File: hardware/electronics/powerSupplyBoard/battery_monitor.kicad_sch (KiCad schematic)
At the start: 34 parts, among them J10 1729018, J9 S3B-XH-SM4-TB, Q2 CSD18532Q5B, Q3 CSD18532Q5B, U5 BQ76905

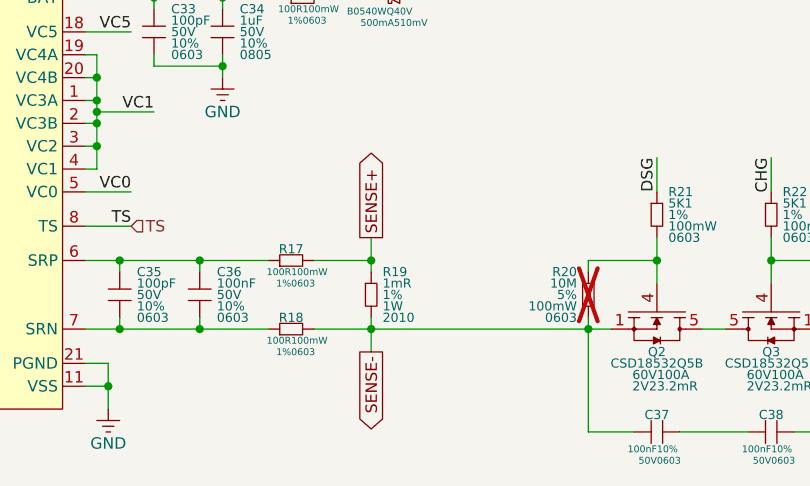
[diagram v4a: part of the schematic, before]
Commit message: recalculated Rsense
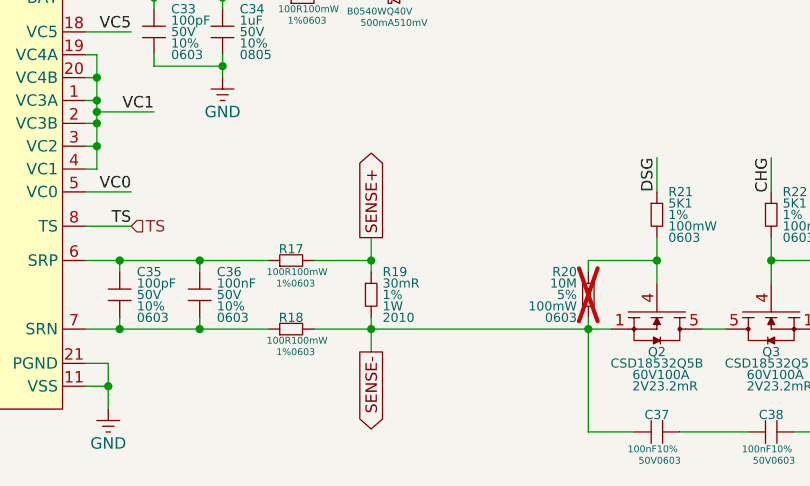
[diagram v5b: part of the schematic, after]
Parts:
- R19: value 1mR -> 30mR; DKPN WSLF-.001CT-ND -> WSLF-.03CT-ND; MPN WSL20101L000FEA18 -> WSL2010R0300FEA18
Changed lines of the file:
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@@
 	)
 	(symbol
-		(lib_id "lib_sch:R")
-		(at 158.75 121.92 0)
-		(unit 1)
-		(exclude_from_sim no)
-		(in_bom yes)
-		(on_board yes)
-		(dnp no)
-		(property "Reference" "R19"
-			(at 160.02 119.38 0)
-			(do_not_autoplace yes)
-			(effects
-				(font
-					(size 1.016 1.016)
-				)
-				(justify left)
-			)
-		)
-		(property "Value" "1mR"
-			(at 160.02 120.65 0)
-			(do_not_autoplace yes)
-			(effects
-				(font
-					(size 1.016 1.016)
-				)
-				(justify left)
-			)
-		)
-		(property "Footprint" "DS-Resistors-SMD:WSLHP2010"
-			(at 158.75 119.38 0)
-			(effects
-				(font
-					(size 1.27 1.27)
-				)
-				(hide yes)
-			)
-		)
-		(property "Datasheet" "datasheets/Vishay-Dale-WSL-HP.pdf"
-			(at 158.75 119.38 0)
-			(effects
-				(font
-					(size 1.27 1.27)
-				)
-				(hide yes)
-			)
-		)
-		(property "Description" "RES 0.001 OHM 1% 1W 2010"
-			(at 158.75 121.92 0)
-			(effects
-				(font
-					(size 1.27 1.27)
-				)
-				(hide yes)
-			)
-		)
-		(property "Manufacturer" "Vishay Dale"
-			(at 158.75 119.38 0)
-			(effects
-				(font
-					(size 1.27 1.27)
-				)
-				(hide yes)
-			)
-		)
-		(property "MPN" "WSL20101L000FEA18"
-			(at 158.75 119.38 0)
-			(effects
-				(font
-					(size 1.27 1.27)
-				)
-				(hide yes)
-			)
-		)
-		(property "DKPN" "WSLF-.001CT-ND"
-			(at 158.75 121.92 0)
-			(effects
-				(font
-					(size 1.27 1.27)
-				)
-				(hide yes)
-			)
-		)
-		(property "Tolerance" "1%"
-			(at 160.02 121.92 0)
-			(do_not_autoplace yes)
-			(effects
-				(font
-					(size 1.016 1.016)
-				)
-				(justify left)
-			)
-		)
-		(property "Power Rating" "1W"
-			(at 160.02 123.19 0)
-			(do_not_autoplace yes)
-			(effects
-				(font
-					(size 1.016 1.016)
-				)
-				(justify left)
-			)
-		)
-		(property "Package" "2010"
-			(at 160.02 124.46 0)
-			(do_not_autoplace yes)
-			(effects
-				(font
-					(size 1.016 1.016)
-				)
-				(justify left)
-			)
-		)
-		(pin "1"
-		)
-		(pin "2"
-		)
-		(instances
-			(project "powerSupplyBoard"
-				(path "/6f3ae1d2-e925-4178-b812-ea14ec542b6c/ec26ef98-8e8c-46d6-a822-e7ed17aae681"
-					(reference "R19")
-					(unit 1)
-				)
-			)
-		)
-	)
-	(symbol
 		(lib_id "lib_sch:GND")
 		(at 81.28 99.06 0)
@@
 					(unit 1)
 				)
+			)
+		)
+	)
+	(symbol
+		(lib_id "lib_sch:R")
+		(at 158.75 121.92 0)
+		(unit 1)
+		(exclude_from_sim no)
+		(in_bom yes)
+		(on_board yes)
+		(dnp no)
+		(property "Reference" "R19"
+			(at 160.02 119.38 0)
+			(do_not_autoplace yes)
+			(effects
+				(font
+					(size 1.016 1.016)
+				)
+				(justify left)
+			)
+		)
+		(property "Value" "30mR"
+			(at 160.02 120.65 0)
+			(do_not_autoplace yes)
+			(effects
+				(font
+					(size 1.016 1.016)
+				)
+				(justify left)
+			)
+		)
+		(property "Footprint" "DS-Resistors-SMD:WSLHP2010"
+			(at 158.75 119.38 0)
+			(effects
+				(font
+					(size 1.27 1.27)
+				)
+				(hide yes)
+			)
+		)
+		(property "Datasheet" "datasheets/Vishay-Dale-WSL-HP.pdf"
+			(at 158.75 119.38 0)
+			(effects
+				(font
+					(size 1.27 1.27)
+				)
+				(hide yes)
+			)
+		)
+		(property "Description" "RES 0.03 OHM 1% 1W 2010"
+			(at 158.75 121.92 0)
+			(effects
+				(font
+					(size 1.27 1.27)
+				)
+				(hide yes)
+			)
+		)
+		(property "Manufacturer" "Vishay Dale"
+			(at 158.75 119.38 0)
+			(effects
+				(font
+					(size 1.27 1.27)
+				)
+				(hide yes)
+			)
+		)
+		(property "MPN" "WSL2010R0300FEA18"
+			(at 158.75 119.38 0)
+			(effects
+				(font
+					(size 1.27 1.27)
+				)
+				(hide yes)
+			)
+		)
+		(property "DKPN" "WSLF-.03CT-ND"
+			(at 158.75 121.92 0)
+			(effects
+				(font
+					(size 1.27 1.27)
+				)
+				(hide yes)
+			)
+		)
+		(property "Tolerance" "1%"
+			(at 160.02 121.92 0)
+			(do_not_autoplace yes)
+			(effects
+				(font
+					(size 1.016 1.016)
+				)
+				(justify left)
+			)
+		)
+		(property "Power Rating" "1W"
+			(at 160.02 123.19 0)
+			(do_not_autoplace yes)
+			(effects
+				(font
+					(size 1.016 1.016)
+				)
+				(justify left)
+			)
+		)
+		(property "Package" "2010"
+			(at 160.02 124.46 0)
+			(do_not_autoplace yes)
+			(effects
+				(font
+					(size 1.016 1.016)
+				)
+				(justify left)
+			)
+		)
+		(pin "1"
+		)
+		(pin "2"
+		)
+		(instances
+			(project "powerSupplyBoard"
+				(path "/6f3ae1d2-e925-4178-b812-ea14ec542b6c/ec26ef98-8e8c-46d6-a822-e7ed17aae681"
+					(reference "R19")
+					(unit 1)
+				)

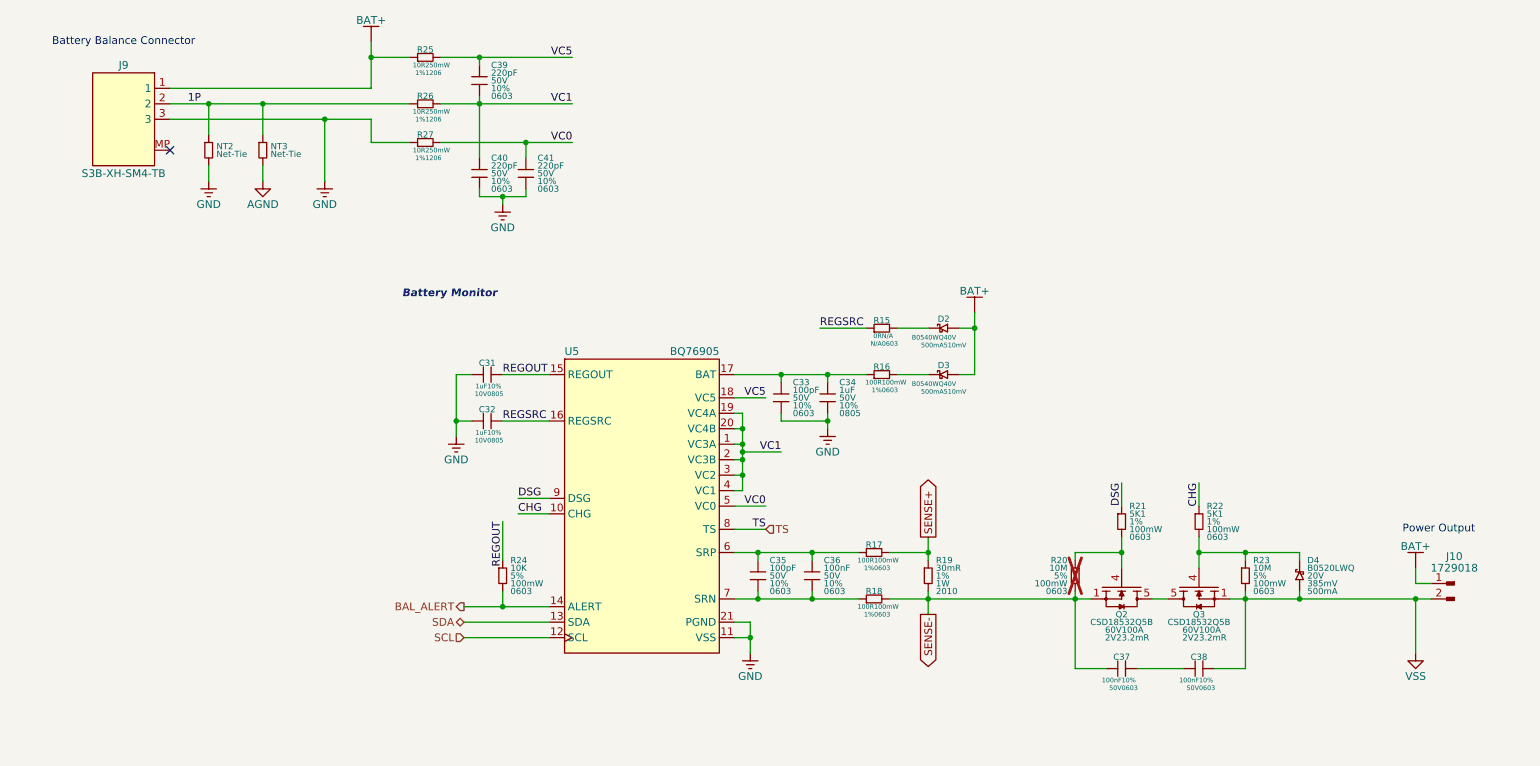
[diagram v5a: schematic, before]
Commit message: added block titles and fixed component properties
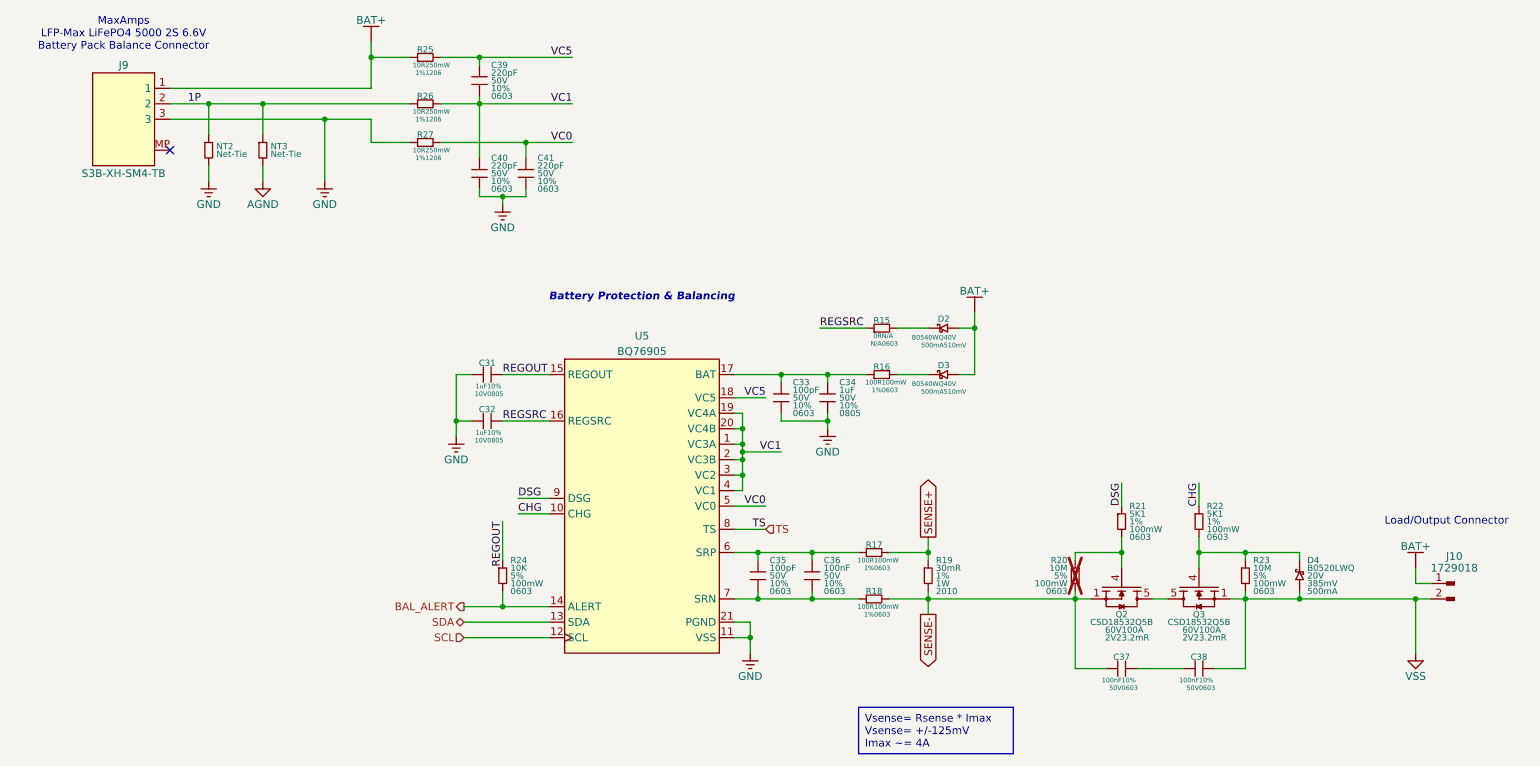
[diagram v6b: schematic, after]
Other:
- note added: "Battery Protection & Balancing"
- note added: "Load/Output Connector"
- note added: "MaxAmps LFP-Max LiFePO4 5000 2S 6.6V Battery Pack Balance Connector"
- note removed: "Battery Balance Connector"
- note removed: "Battery Monitor"
- note removed: "Power Output"
- title: LiFePO4 Monitor & Balancer -> LiFePO4 Protection & Balancer
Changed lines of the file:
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@@
 	(paper "USLetter")
 	(title_block
-		(title "LiFePO4 Monitor & Balancer")
-		(date "2024-11-01")
+		(title "LiFePO4 Protection & Balancer")
+		(date "2024-11-03")
 		(rev "01")
 		(comment 2 "PROTOTYPE")
@@
 		)
 	)
-	(text "Power Output"
+	(text_box "Vsense= Rsense * Imax\nVsense= +/-125mV\nImax ~= 4A"
 		(exclude_from_sim no)
-		(at 242.57 114.3 0)
+		(at 147.32 143.51 0)
+		(size 25.4 7.62)
+		(stroke
+			(width 0)
+			(type default)
+		)
+		(fill
+			(type none)
+		)
+		(effects
+			(font
+				(size 1.27 1.27)
+			)
+			(justify left top)
+		)
+	)
+	(text "Load/Output Connector"
+		(exclude_from_sim no)
+		(at 243.84 113.03 0)
 		(effects
 			(font
@@
 		)
 	)
-	(text "Battery Balance Connector"
+	(text "MaxAmps\nLFP-Max LiFePO4 5000 2S 6.6V\nBattery Pack Balance Connector"
 		(exclude_from_sim no)
-		(at 26.67 34.29 0)
+		(at 26.67 33.02 0)
 		(effects
 			(font
@@
 		)
 	)
-	(text "Battery Monitor"
+	(text "Battery Protection & Balancing"
 		(exclude_from_sim no)
-		(at 72.39 75.692 0)
+		(at 111.76 76.2 0)
 		(effects
 			(font
@@
 				(italic yes)
 			)
-			(justify left)
 		)
 	)
@@
 			)
 		)
-		(property "Description" ""
+		(property "Description" "CAP CER 0.1UF 50V X7R 0603"
 			(at 203.2 137.16 0)
 			(effects
@@
 			)
 		)
-		(property "Description" ""
+		(property "Description" "CAP CER 0.1UF 50V X7R 0603"
 			(at 190.5 137.16 0)
 			(effects
@@
 		(on_board yes)
 		(dnp no)
-		(fields_autoplaced yes)
 		(property "Reference" "U5"
-			(at 99.06 85.09 0)
+			(at 111.76 82.55 0)
 			(do_not_autoplace yes)
 			(effects
@@
 					(size 1.27 1.27)
 				)
-				(justify left)
 			)
 		)
 		(property "Value" "BQ76905"
-			(at 124.46 85.09 0)
+			(at 111.76 85.09 0)
 			(do_not_autoplace yes)
 			(effects
@@
 					(size 1.27 1.27)
 				)
-				(justify right)
 			)
 		)
@@
 			)
 		)
-		(property "Description" "Ceramic capacitor symbol"
+		(property "Description" "CAP CER 0.1UF 50V X7R 0603"
 			(at 139.7 121.92 0)
 			(effects

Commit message: redefined footprint paths
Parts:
- C31, C32, C34: footprint DS-Capacitors-SMD:MLCC0805 -> lib_fp:MLCC0805
- C33, C35, C39, C40, C41: footprint DS-Capacitors-SMD:MLCC0603 -> lib_fp:MLCC0603
- C36, C37, C38: footprint DS-Capacitors-SMD:MLCC0603 -> lib_fp:MLCC0603; MPN 06035C104K4T4A -> KAM15AR71H104KM
- D2, D3, D4: footprint DS-Package-SO:SOD123 -> lib_fp:SOD123
- J10: footprint DS-Rectangular-Connectors:5mmTerminalBlock -> lib_fp:5mmTerminalBlock
- J9: footprint DS-Rectangular-Connectors:JST_XH_S3B-SM4-TB -> lib_fp:JST_XH_S3B-SM4-TB
- NT2, NT3: footprint DS-Resistors-SMD:CRCW1210 -> lib_fp:CRCW2010
- Q2, Q3: footprint DS-Package-SO:SON8P127_500X600X100L56X41N -> lib_fp:SON8P127_500X600X100L56X41N
- R15, R16, R17, R18, R20, R21, R22, R23, R24: footprint DS-Resistors-SMD:CRCW0603 -> lib_fp:CRCW0603
- R19: footprint DS-Resistors-SMD:WSLHP2010 -> lib_fp:WSLHP2010
- R25, R26, R27: footprint DS-Resistors-SMD:CRCW1206 -> lib_fp:CRCW1206
- U5: footprint DS-PMIC-SMD:RGR0020A -> lib_fp:RGR0020A
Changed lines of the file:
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@@
 			)
 		)
-		(property "Footprint" "DS-Resistors-SMD:CRCW1210"
+		(property "Footprint" "lib_fp:CRCW2010"
 			(at 49.53 49.53 0)
 			(effects
@@
 			)
 		)
-		(property "Footprint" "DS-Resistors-SMD:CRCW0603"
+		(property "Footprint" "lib_fp:CRCW0603"
 			(at 203.2 110.49 0)
 			(effects
@@
 			)
 		)
-		(property "Footprint" "DS-Capacitors-SMD:MLCC0603"
+		(property "Footprint" "lib_fp:MLCC0603"
 			(at 203.2 142.875 0)
 			(effects
@@
 			)
 		)
-		(property "MPN" "06035C104K4T4A"
+		(property "MPN" "KAM15AR71H104KM"
 			(at 203.2 142.875 0)
 			(effects
@@
 			)
 		)
-		(property "Footprint" "DS-Capacitors-SMD:MLCC0603"
+		(property "Footprint" "lib_fp:MLCC0603"
 			(at 134.62 90.805 0)
 			(effects
@@
 			)
 		)
-		(property "Footprint" "DS-Resistors-SMD:CRCW0603"
+		(property "Footprint" "lib_fp:CRCW0603"
 			(at 147.32 118.11 90)
 			(effects
@@
 			)
 		)
-		(property "Footprint" "DS-Capacitors-SMD:MLCC0805"
+		(property "Footprint" "lib_fp:MLCC0805"
 			(at 142.24 90.805 0)
 			(effects
@@
 			)
 		)
-		(property "Footprint" "DS-Resistors-SMD:CRCW1210"
+		(property "Footprint" "lib_fp:CRCW2010"
 			(at 40.64 49.53 0)
 			(effects
@@
 			)
 		)
-		(property "Footprint" "DS-Capacitors-SMD:MLCC0603"
+		(property "Footprint" "lib_fp:MLCC0603"
 			(at 130.81 120.015 0)
 			(effects
@@
 			)
 		)
-		(property "Footprint" "DS-Resistors-SMD:CRCW0603"
+		(property "Footprint" "lib_fp:CRCW0603"
 			(at 148.59 88.9 90)
 			(effects
@@
 			)
 		)
-		(property "Footprint" "DS-Capacitors-SMD:MLCC0603"
+		(property "Footprint" "lib_fp:MLCC0603"
 			(at 190.5 142.875 0)
 			(effects
@@
 			)
 		)
-		(property "MPN" "06035C104K4T4A"
+		(property "MPN" "KAM15AR71H104KM"
 			(at 190.5 142.875 0)
 			(effects
@@
 			)
 		)
-		(property "Footprint" "DS-Resistors-SMD:CRCW0603"
+		(property "Footprint" "lib_fp:CRCW0603"
 			(at 88.9 119.38 0)
 			(effects
@@
 			)
 		)
-		(property "Footprint" "DS-Package-SO:SOD123"
+		(property "Footprint" "lib_fp:SOD123"
 			(at 219.71 121.92 90)
 			(effects
@@
 			)
 		)
-		(property "Footprint" "DS-Capacitors-SMD:MLCC0603"
+		(property "Footprint" "lib_fp:MLCC0603"
 			(at 85.09 38.735 0)
 			(effects
@@
 			)
 		)
-		(property "Footprint" "DS-Resistors-SMD:CRCW1206"
+		(property "Footprint" "lib_fp:CRCW1206"
 			(at 73.66 50.8 90)
 			(effects
@@
 			)
 		)
-		(property "Footprint" "DS-Resistors-SMD:CRCW0603"
+		(property "Footprint" "lib_fp:CRCW0603"
 			(at 147.32 125.73 90)
 			(effects
@@
 			)
 		)
-		(property "Footprint" "DS-Resistors-SMD:CRCW1206"
+		(property "Footprint" "lib_fp:CRCW1206"
 			(at 73.66 44.45 90)
 			(effects
@@
 			)
 		)
-		(property "Footprint" "DS-Package-SO:SOD123"
+		(property "Footprint" "lib_fp:SOD123"
 			(at 161.29 88.9 0)
 			(effects
@@
 			)
 		)
-		(property "Footprint" "DS-Capacitors-SMD:MLCC0805"
+		(property "Footprint" "lib_fp:MLCC0805"
 			(at 86.36 102.235 0)
 			(effects
@@
 			)
 		)
-		(property "Footprint" "DS-PMIC-SMD:RGR0020A"
+		(property "Footprint" "lib_fp:RGR0020A"
 			(at 127 101.6 0)
 			(effects
@@
 			)
 		)
-		(property "Footprint" "DS-Resistors-SMD:CRCW0603"
+		(property "Footprint" "lib_fp:CRCW0603"
 			(at 182.88 119.38 0)
 			(effects
@@
 			)
 		)
-		(property "Footprint" "DS-Resistors-SMD:CRCW0603"
+		(property "Footprint" "lib_fp:CRCW0603"
 			(at 148.59 81.28 90)
 			(effects
@@
 			)
 		)
-		(property "Footprint" "DS-Package-SO:SOD123"
+		(property "Footprint" "lib_fp:SOD123"
 			(at 161.29 81.28 0)
 			(effects
@@
 			)
 		)
-		(property "Footprint" "DS-Resistors-SMD:CRCW0603"
+		(property "Footprint" "lib_fp:CRCW0603"
 			(at 210.82 119.38 0)
 			(effects
@@
 			)
 		)
-		(property "Footprint" "DS-Capacitors-SMD:MLCC0603"
+		(property "Footprint" "lib_fp:MLCC0603"
 			(at 139.7 120.015 0)
 			(effects
@@
 			)
 		)
-		(property "MPN" "06035C104K4T4A"
+		(property "MPN" "KAM15AR71H104KM"
 			(at 139.7 120.015 0)
 			(effects
@@
 			)
 		)
-		(property "Footprint" "DS-Capacitors-SMD:MLCC0603"
+		(property "Footprint" "lib_fp:MLCC0603"
 			(at 92.71 53.975 0)
 			(effects
@@
 			)
 		)
-		(property "Footprint" "DS-Rectangular-Connectors:5mmTerminalBlock"
+		(property "Footprint" "lib_fp:5mmTerminalBlock"
 			(at 243.84 125.73 0)
 			(effects
@@
 			)
 		)
-		(property "Footprint" "DS-Package-SO:SON8P127_500X600X100L56X41N"
+		(property "Footprint" "lib_fp:SON8P127_500X600X100L56X41N"
 			(at 205.105 128.27 90)
 			(effects
@@
 			)
 		)
-		(property "Footprint" "DS-Resistors-SMD:CRCW0603"
+		(property "Footprint" "lib_fp:CRCW0603"
 			(at 190.5 110.49 0)
 			(effects
@@
 			)
 		)
-		(property "Footprint" "DS-Resistors-SMD:CRCW1206"
+		(property "Footprint" "lib_fp:CRCW1206"
 			(at 73.66 36.83 90)
 			(effects
@@
 			)
 		)
-		(property "Footprint" "DS-Capacitors-SMD:MLCC0805"
+		(property "Footprint" "lib_fp:MLCC0805"
 			(at 86.36 94.615 0)
 			(effects
@@
 			)
 		)
-		(property "Footprint" "DS-Resistors-SMD:WSLHP2010"
+		(property "Footprint" "lib_fp:WSLHP2010"
 			(at 158.75 119.38 0)
 			(effects
@@
 			)
 		)
-		(property "Footprint" "DS-Capacitors-SMD:MLCC0603"
+		(property "Footprint" "lib_fp:MLCC0603"
 			(at 85.09 53.975 0)
 			(effects
@@
 			)
 		)
-		(property "Footprint" "DS-Rectangular-Connectors:JST_XH_S3B-SM4-TB"
+		(property "Footprint" "lib_fp:JST_XH_S3B-SM4-TB"
 			(at 31.75 39.37 0)
 			(effects
@@
 			)
 		)
-		(property "Footprint" "DS-Package-SO:SON8P127_500X600X100L56X41N"
+		(property "Footprint" "lib_fp:SON8P127_500X600X100L56X41N"
 			(at 188.595 128.27 90)
 			(effects
